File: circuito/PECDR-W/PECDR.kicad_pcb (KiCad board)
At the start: 4 copper layers, 85 x 54 mm, 68 parts, among them J1 O2, J10 GP-SPI, J11 GP-SPI, J12 O3, J13 GND, J14 A, J15 B, J16 VS-SELECT, J17 GP-I2C1, J2 O4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

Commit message: PECDR update
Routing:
- net +3V3: track 228.1 -> 229.2 mm
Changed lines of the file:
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@@
   (segment (start 37.175 89.127944) (end 37.02 89.282944) (width 0.5) (layer "B.Cu") (net 2))
   (segment (start 106.175 87.627944) (end 105.7 87.152944) (width 0.5) (layer "B.Cu") (net 2))
-  (segment (start 88.9505 76.602944) (end 90 76.602944) (width 1.5) (layer "B.Cu") (net 2))
   (segment (start 105.7 87.152944) (end 105.7 82.502944) (width 0.5) (layer "B.Cu") (net 2))
   (segment (start 98.75 75.552944) (end 98.75 66.552944) (width 0.5) (layer "B.Cu") (net 2))
@@
   (segment (start 47.59 68.882944) (end 49.17 67.302944) (width 1.5) (layer "B.Cu") (net 2))
   (segment (start 92.4 79.282944) (end 90 81.682944) (width 1.5) (layer "B.Cu") (net 2))
+  (segment (start 87.9 76.402944) (end 89.8 76.402944) (width 0.8) (layer "B.Cu") (net 2))
   (segment (start 84.1 65.702944) (end 87.2 68.802944) (width 1.5) (layer "B.Cu") (net 2))
   (segment (start 37.7 103.302944) (end 49.17 103.302944) (width 0.5) (layer "B.Cu") (net 2))
@@
   (segment (start 95 68.802944) (end 98 65.802944) (width 1.5) (layer "B.Cu") (net 2))
   (segment (start 40.925 73.902944) (end 40.925 72.787944) (width 0.5) (layer "B.Cu") (net 2))
+  (segment (start 89.8 76.402944) (end 90 76.602944) (width 0.8) (layer "B.Cu") (net 2))
   (segment (start 36.96 86.802944) (end 37.02 86.742944) (width 0.5) (layer "B.Cu") (net 4))
   (segment (start 34.8 86.802944) (end 36.96 86.802944) (width 0.5) (layer "B.Cu") (net 4))
@@
   (segment (start 85.5 79.602944) (end 85.5 81.702944) (width 0.5) (layer "B.Cu") (net 55))
   (zone (net 1) (net_name "GND") (layers "F.Cu" "In1.Cu" "In2.Cu" "B.Cu") (name "VS") (hatch edge 0.5)
+    (priority 2)
+    (connect_pads yes (clearance 0.4))
+    (min_thickness 0.3) (filled_areas_thickness no)
+    (fill yes (thermal_gap 0.5) (thermal_bridge_width 0.4) (smoothing chamfer) (radius 0.5) (island_removal_mode 1) (island_area_min 10))
+    (polygon
+      (pts
+        (xy 39.6 93.202944)
+        (xy 39.6 101.202944)
+        (xy 47.6 101.202944)
+        (xy 47.6 93.202944)
+      )
+    )
+  )
+  (zone (net 1) (net_name "GND") (layers "F.Cu" "In1.Cu" "In2.Cu" "B.Cu") (name "VS") (hatch edge 0.5)
     (priority 1)
     (connect_pads yes (clearance 0.4))
@@
       )
     )
+  )
+  (zone (net 1) (net_name "GND") (layers "F.Cu" "In1.Cu" "In2.Cu" "B.Cu") (name "VS") (hatch edge 0.5)
+    (priority 2)
+    (connect_pads yes (clearance 0.4))
+    (min_thickness 0.3) (filled_areas_thickness no)
+    (fill yes (thermal_gap 0.5) (thermal_bridge_width 0.4) (smoothing chamfer) (radius 0.5) (island_removal_mode 1) (island_area_min 10))
+    (polygon
+      (pts
+        (xy 39.5 59.502944)
+        (xy 39.5 67.502944)
+        (xy 47.5 67.502944)
+        (xy 47.5 59.502944)
+      )
+    )

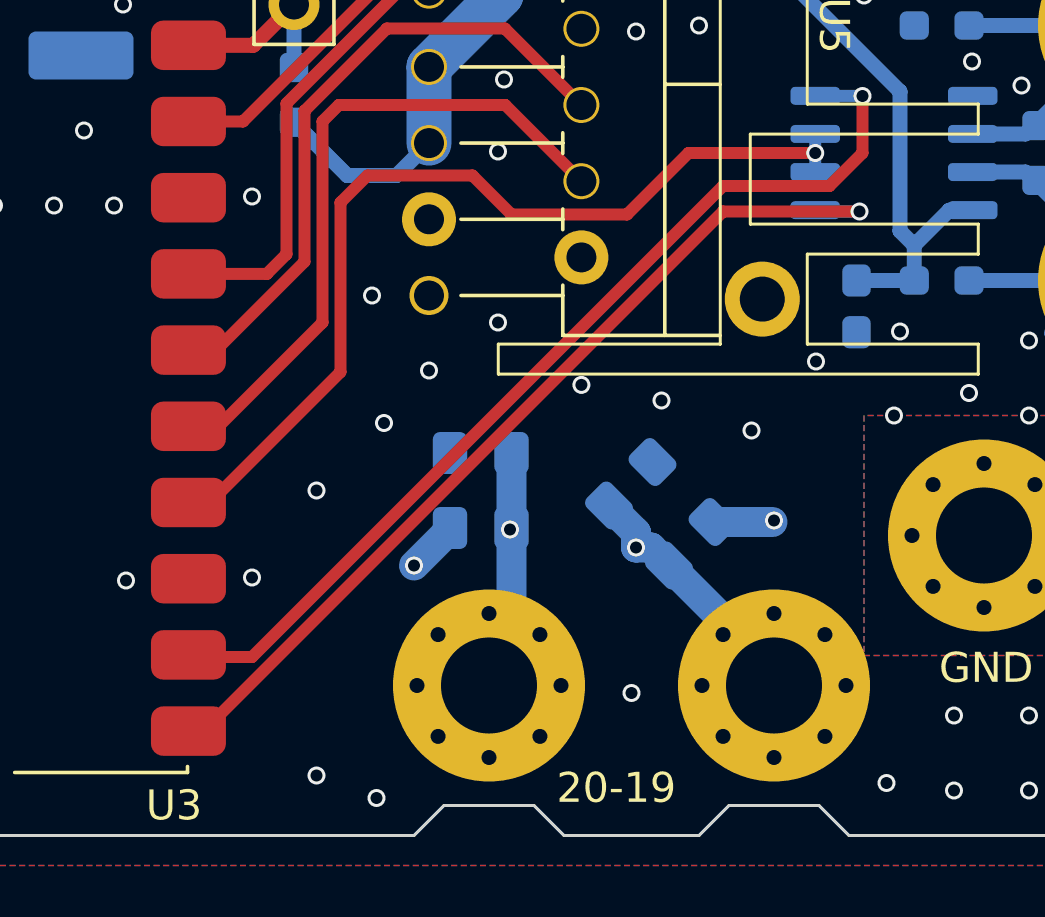
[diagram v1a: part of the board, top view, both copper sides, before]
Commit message: anotando correções em PECDR-W e criando programa de testes
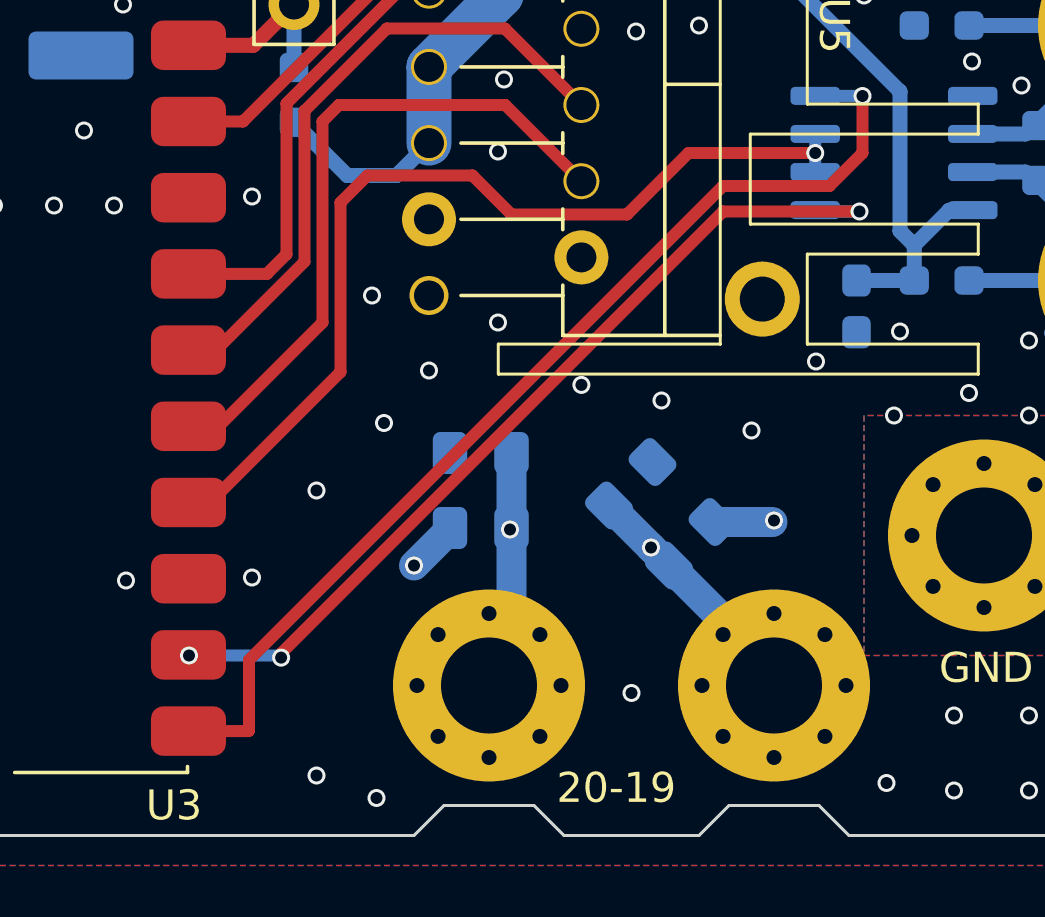
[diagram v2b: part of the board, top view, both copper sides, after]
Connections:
- U3 pad 21: /ReceiverOutput -> /DriverInput
- U3 pad 22: /DriverInput -> /ReceiverOutput
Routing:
- net /DriverInput: track 33.0 -> 36.3 mm
- net /ReceiverOutput: track 31.0 -> 30.2 mm, vias 1 -> 3
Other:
- board text added: "colocar os pinos não usados como smd por baixo se possivel manter passo de 2.54"
- board text added: "colocar um afastamento de GND na região dos connectores de potência"
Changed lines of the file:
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@@
       (net 29 "/G15") (pinfunction "GP15") (pintype "bidirectional"))
     (pad "21" smd roundrect (at 21.032 -1.38) (size 2.5 1.65) (layers "F.Cu" "F.Paste" "F.Mask") (roundrect_rratio 0.25)
-      (net 19 "/ReceiverOutput") (pinfunction "GP16") (pintype "bidirectional"))
+      (net 21 "/DriverInput") (pinfunction "GP16") (pintype "bidirectional"))
     (pad "22" smd roundrect (at 21.032 -3.92) (size 2.5 1.65) (layers "F.Cu" "F.Paste" "F.Mask") (roundrect_rratio 0.25)
-      (net 21 "/DriverInput") (pinfunction "GP17") (pintype "bidirectional"))
+      (net 19 "/ReceiverOutput") (pinfunction "GP17") (pintype "bidirectional"))
     (pad "23" smd roundrect (at 21.032 -6.46) (size 2.5 1.65) (layers "F.Cu" "F.Paste" "F.Mask") (roundrect_rratio 0.25)
       (net 1 "GND") (pinfunction "GND") (pintype "passive"))
@@
     (effects (font (size 1 1) (thickness 0.15)) (justify left bottom))
   )
+  (gr_text "colocar um afastamento de GND\nna região dos connectores de\npotência" (at 125.1 80.102944 90) (layer "Dwgs.User")
+    (effects (font (size 1 1) (thickness 0.2) bold) (justify bottom))
+  )
+  (gr_text "colocar os pinos não usados\ncomo smd por baixo se possivel\nmanter passo  de 2.54" (at 69.3 82.702944) (layer "Dwgs.User")
+    (effects (font (size 1 1) (thickness 0.2) bold) (justify bottom))
+  )
   (dimension (type aligned) (layer "Cmts.User")
     (pts (xy 43.5 63.302944) (xy 33.5 63.302944))
@@
   (segment (start 92.75 97.152944) (end 92.75 101.552944) (width 1) (layer "B.Cu") (net 11))
   (via (at 95.08 92.282944) (size 0.6) (drill 0.4) (layers "F.Cu" "B.Cu") (net 12))
-  (via (at 96.9 97.702944) (size 0.6) (drill 0.4) (layers "F.Cu" "B.Cu") (net 12))
+  (via (at 97.4 97.702944) (size 0.6) (drill 0.4) (layers "F.Cu" "B.Cu") (net 12))
   (segment (start 95.08 92.282944) (end 95.08 95.882944) (width 2.35) (layer "In1.Cu") (net 12))
   (segment (start 95.08 95.882944) (end 101.5 102.302944) (width 2.35) (layer "In1.Cu") (net 12))
@@
   (segment (start 95.08 88.032944) (end 95.08 95.882944) (width 2.35) (layer "In2.Cu") (net 12))
   (segment (start 95.08 95.882944) (end 101.5 102.302944) (width 2.35) (layer "In2.Cu") (net 12))
-  (segment (start 99.802944 100.105888) (end 99.802944 100.605888) (width 1) (layer "B.Cu") (net 12))
-  (segment (start 96.9 97.702944) (end 97.4 97.702944) (width 1) (layer "B.Cu") (net 12))
-  (segment (start 98 98.302944) (end 101.5 101.802944) (width 1) (layer "B.Cu") (net 12))
   (segment (start 97.4 97.702944) (end 99.802944 100.105888) (width 1) (layer "B.Cu") (net 12))
-  (segment (start 96.9 97.702944) (end 96.9 97.202944) (width 1) (layer "B.Cu") (net 12))
-  (segment (start 96.9 97.202944) (end 96 96.302944) (width 1) (layer "B.Cu") (net 12))
+  (segment (start 97.4 97.702944) (end 96 96.302944) (width 1) (layer "B.Cu") (net 12))
+  (segment (start 98 98.302944) (end 101.5 101.802944) (width 1) (layer "B.Cu") (net 12))
+  (segment (start 99.802944 100.105888) (end 99.802944 100.605888) (width 1) (layer "B.Cu") (net 12))
   (segment (start 101.5 101.802944) (end 101.5 102.302944) (width 1) (layer "B.Cu") (net 12))
   (segment (start 76.9995 77.352944) (end 79.15 77.352944) (width 0.5) (layer "F.Cu") (net 13))
@@
   (segment (start 99.449568 96.853376) (end 101.449568 96.853376) (width 1) (layer "B.Cu") (net 18))
   (segment (start 90.7 63.002944) (end 88.25 60.552944) (width 1) (layer "B.Cu") (net 18))
-  (segment (start 99.8 86.502944) (end 82.48 103.822944) (width 0.4) (layer "F.Cu") (net 19))
-  (segment (start 104.35 86.502944) (end 99.8 86.502944) (width 0.4) (layer "F.Cu") (net 19))
-  (segment (start 82.48 103.822944) (end 81.982 103.822944) (width 0.4) (layer "F.Cu") (net 19))
+  (segment (start 82 101.300944) (end 81.982 101.282944) (width 0.4) (layer "F.Cu") (net 19))
+  (segment (start 82.002 101.302944) (end 82 101.302944) (width 0.4) (layer "F.Cu") (net 19))
+  (segment (start 82 101.302944) (end 82 101.300944) (width 0.4) (layer "F.Cu") (net 19))
+  (segment (start 85.070711 101.232233) (end 99.8 86.502944) (width 0.4) (layer "F.Cu") (net 19))
+  (segment (start 85.070711 101.373655) (end 85.070711 101.232233) (width 0.4) (layer "F.Cu") (net 19))
+  (segment (start 81.982 101.282944) (end 82.052 101.352944) (width 0.4) (layer "F.Cu") (net 19))
+  (segment (start 82.002 101.302944) (end 82.002 101.302944) (width 0.4) (layer "F.Cu") (net 19))
+  (segment (start 99.8 86.502944) (end 104.35 86.502944) (width 0.4) (layer "F.Cu") (net 19))
   (via (at 104.35 86.502944) (size 0.6) (drill 0.4) (layers "F.Cu" "B.Cu") (net 19))
+  (via (at 85.070711 101.373655) (size 0.6) (drill 0.4) (layers "F.Cu" "B.Cu") (net 19))
+  (via (at 82 101.302944) (size 0.6) (drill 0.4) (layers "F.Cu" "B.Cu") (net 19))
   (segment (start 104.35 86.502944) (end 102.92 86.502944) (width 0.4) (layer "B.Cu") (net 19))
   (segment (start 102.92 86.502944) (end 102.875 86.457944) (width 0.4) (layer "B.Cu") (net 19))
+  (segment (start 85.070711 101.373655) (end 85 101.302944) (width 0.4) (layer "B.Cu") (net 19))
+  (segment (start 85 101.302944) (end 82 101.302944) (width 0.4) (layer "B.Cu") (net 19))
   (segment (start 87.05 91.852944) (end 82.7 96.202944) (width 0.4) (layer "F.Cu") (net 20))
   (segment (start 87.95 85.302944) (end 87.05 86.202944) (width 0.4) (layer "F.Cu") (net 20))
@@
   (via (at 102.875 84.552944) (size 0.6) (drill 0.4) (layers "F.Cu" "B.Cu") (net 20))
   (segment (start 102.875 85.187944) (end 102.875 83.917944) (width 0.4) (layer "B.Cu") (net 20))
-  (segment (start 84.101472 101.352944) (end 99.801472 85.652944) (width 0.4) (layer "F.Cu") (net 21))
-  (segment (start 99.801472 85.652944) (end 103.35 85.652944) (width 0.4) (layer "F.Cu") (net 21))
-  (segment (start 82.052 101.352944) (end 84.101472 101.352944) (width 0.4) (layer "F.Cu") (net 21))
+  (segment (start 82.98 103.822944) (end 81.982 103.822944) (width 0.4) (layer "F.Cu") (net 21))
+  (segment (start 81.982 103.822944) (end 83.98 103.822944) (width 0.4) (layer "F.Cu") (net 21))
   (segment (start 103.35 85.652944) (end 104.45 84.552944) (width 0.4) (layer "F.Cu") (net 21))
   (segment (start 104.45 84.552944) (end 104.45 82.652944) (width 0.4) (layer "F.Cu") (net 21))
-  (segment (start 81.982 101.282944) (end 82.052 101.352944) (width 0.4) (layer "F.Cu") (net 21))
-  (segment (start 82.002 101.302944) (end 81.982 101.282944) (width 0.4) (layer "F.Cu") (net 21))
+  (segment (start 84 101.454416) (end 99.801472 85.652944) (width 0.4) (layer "F.Cu") (net 21))
+  (segment (start 84 103.802944) (end 84 101.454416) (width 0.4) (layer "F.Cu") (net 21))
+  (segment (start 99.801472 85.652944) (end 103.35 85.652944) (width 0.4) (layer "F.Cu") (net 21))
+  (segment (start 83.98 103.822944) (end 84 103.802944) (width 0.4) (layer "F.Cu") (net 21))
   (via (at 104.45 82.652944) (size 0.6) (drill 0.4) (layers "F.Cu" "B.Cu") (net 21))
   (segment (start 104.445 82.647944) (end 104.45 82.652944) (width 0.4) (layer "B.Cu") (net 21))
@@
       (pts
         (xy 110 75.802944)
-        (xy 117.5 75.802944)
-        (xy 117.5 68.052944)
+        (xy 118.5 75.802944)
+        (xy 118.5 68.052944)
         (xy 107.5 68.052944)
         (xy 103.75 64.652944)

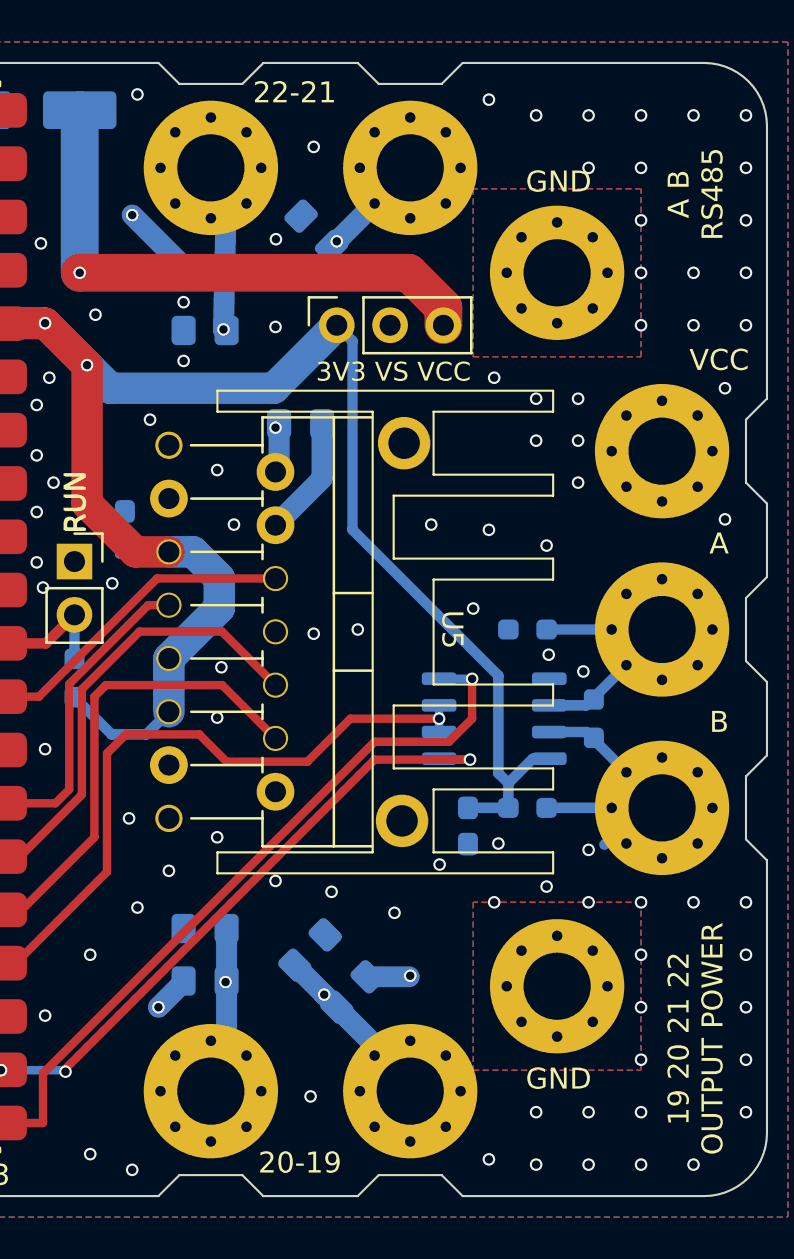
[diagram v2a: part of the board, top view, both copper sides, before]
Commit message: PECDR correção rs485 e de layout
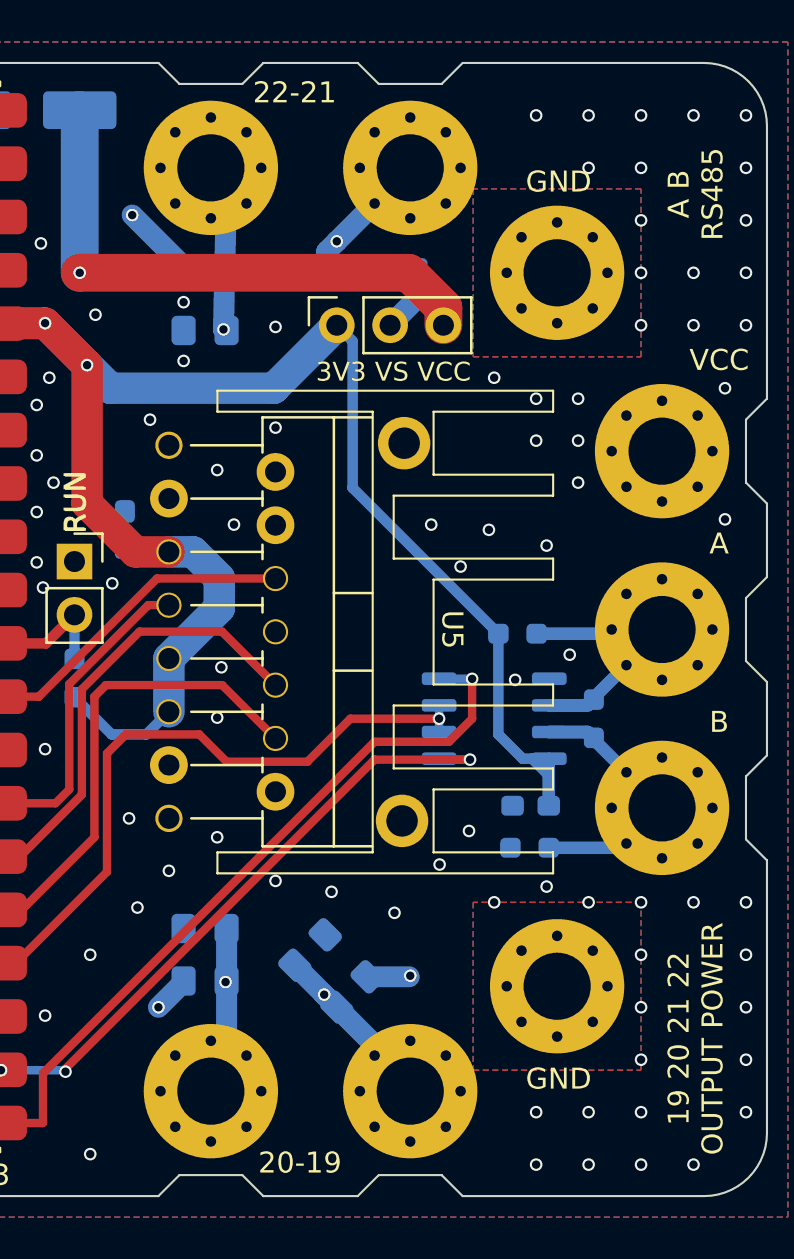
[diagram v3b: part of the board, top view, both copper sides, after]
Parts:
- R1: value 120 -> 4k7
- moved R3 10.4 mm to (107.2, 90.7)
- moved D2 8.46 mm to (100.7, 63.3)
- moved R2 8.31 mm to (106.6, 80.5)
- moved C3 3.14 mm to (107.2, 88.7), turned to 180 degrees
- moved D3 2.04 mm to (96.5, 63.3), turned to 180 degrees
- turned R1 to -90 degrees
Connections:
- R1 pad 1: /B -> /A
- R1 pad 2: /A -> /B
- R2 pad 2: /B -> /A
- R3 pad 1: /A -> /B
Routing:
- net /A: track 10.1 -> 13.9 mm
- net VS: track 25.3 -> 23.1 mm
- net /OUT1: track 39.0 -> 41.0 mm
- net +3V3: track 229.2 -> 227.5 mm
- net /B: track 12.6 -> 14.1 mm
- net GND: vias 158 -> 148
